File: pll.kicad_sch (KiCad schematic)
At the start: 47 parts, among them J201 S353/CDP18U42P, Q201 DTC143ZE, Q202 DTC143ZE, Q203 DTC143ZE, Q204 DTC143ZE, Q205 DTC143ZE, Q206 DTC143ZE, Q207 DTC143ZE, Q208 DTC143ZE, Q209 DTC143ZE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

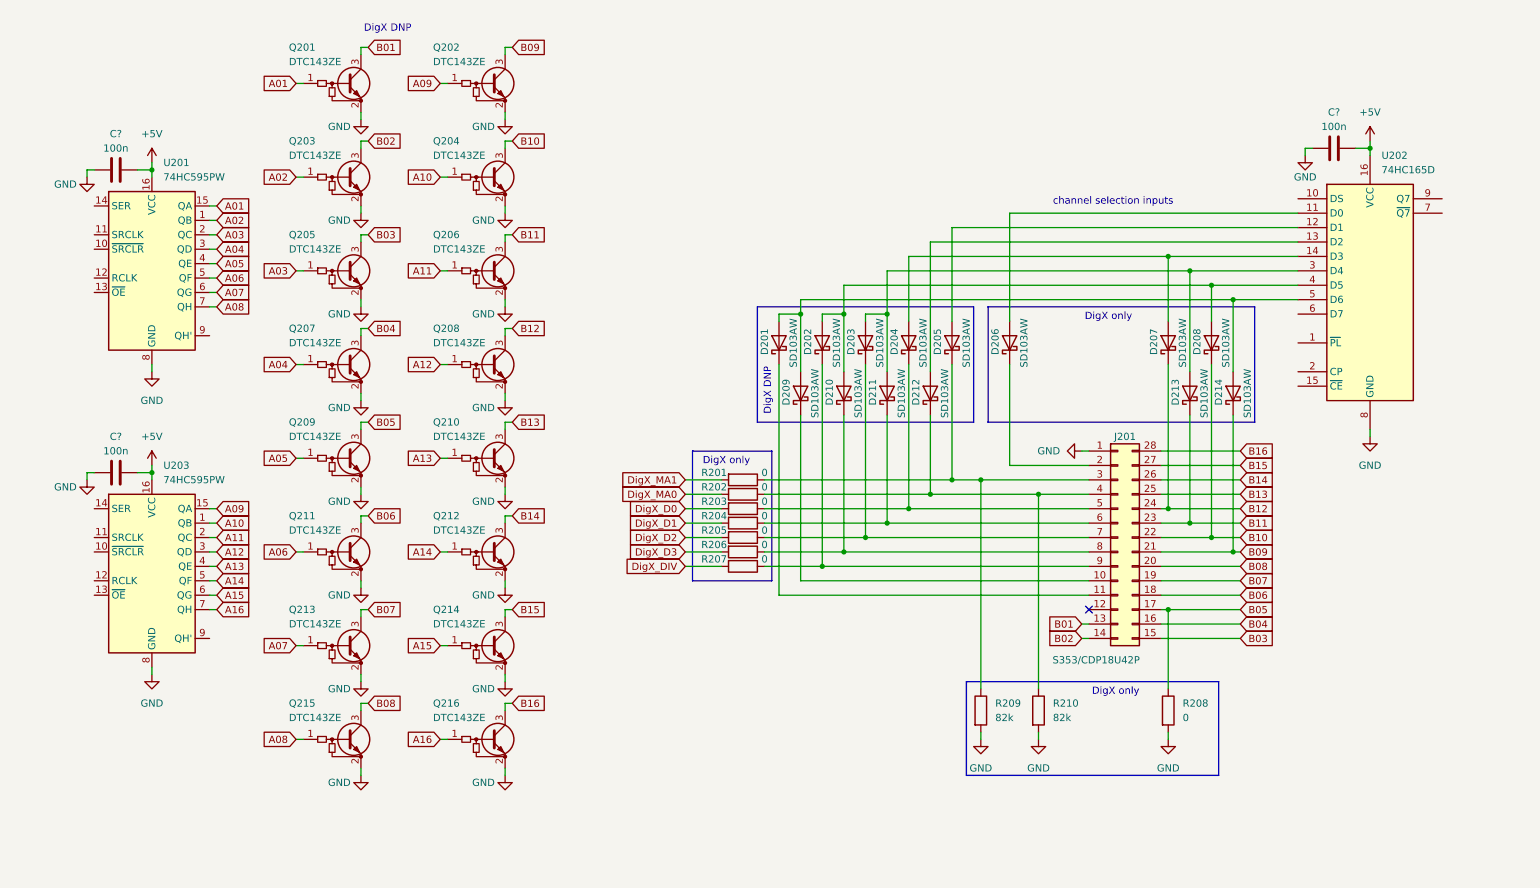
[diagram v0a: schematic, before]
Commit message: Initial TGA-connector, ESP32 and NF-filter circuit.
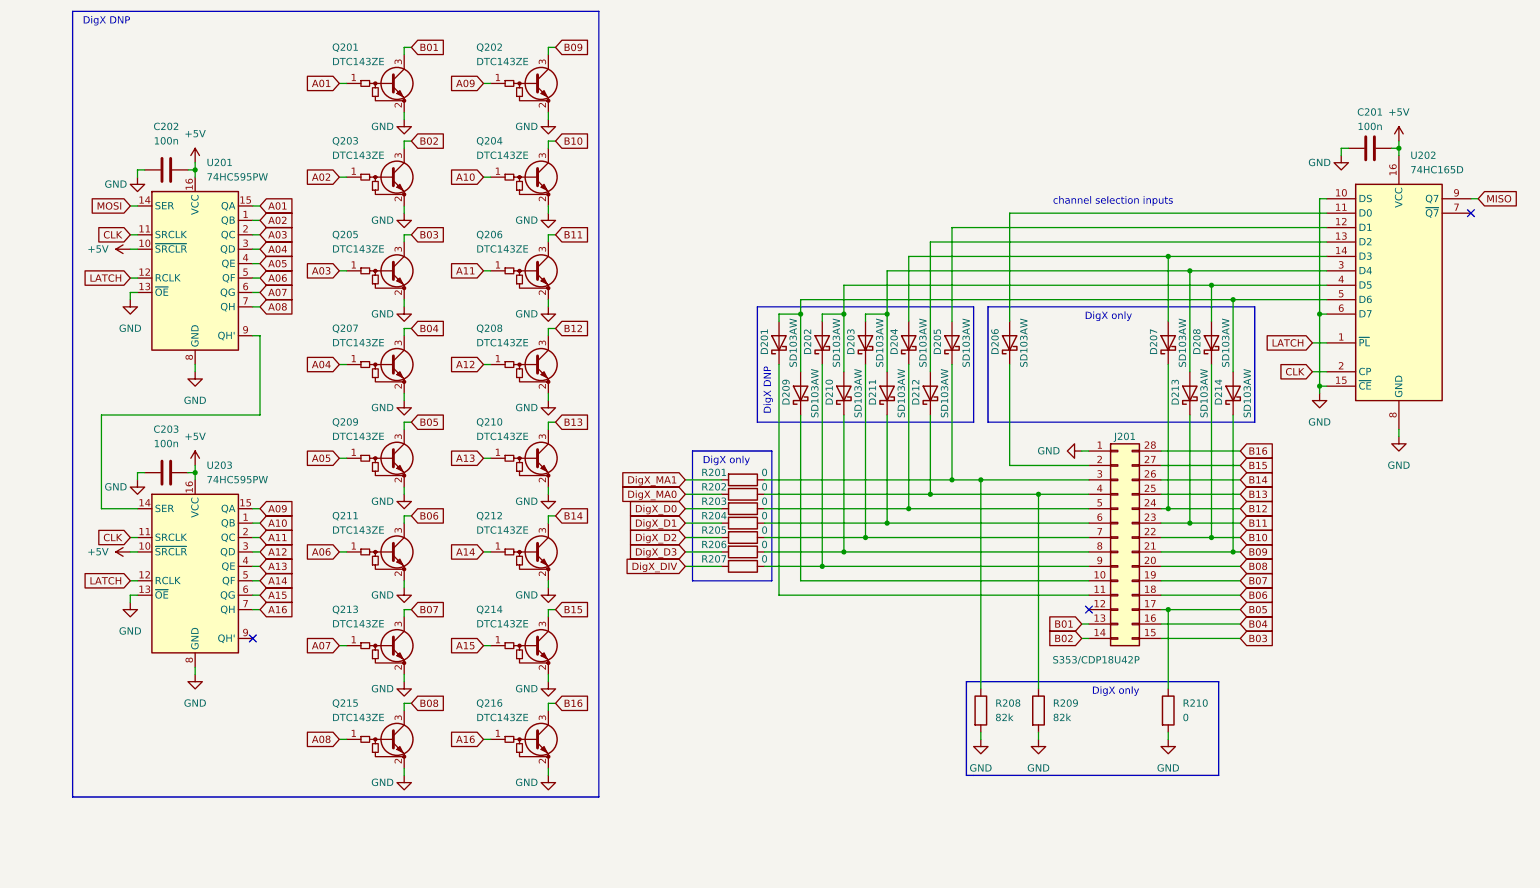
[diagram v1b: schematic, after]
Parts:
- removed C? (x2): 100n, Capacitor_SMD:C_0603_1608Metric, symbol Device:C
- added C202, C203: 100n, Capacitor_SMD:C_0603_1608Metric, symbol Device:C
- gave numbers to parts that had none: 1
- renumbered R209 to R208, R210 to R209, R208 to R210
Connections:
- net +5V: now also U201.10 (~{SRCLR}), U203.10 (~{SRCLR}), C202.2, C203.2
- net GND: now also U201.13 (~{OE}), U202.10 (DS), U202.15 (~{CE}), U202.6 (D7), U203.13 (~{OE}), C202.1, C203.1
- net CLK: now reaches U201.11 (SRCLK)
- net CLK: now also U202.2 (CP), U203.11 (SRCLK)
- net LATCH: now reaches U201.12 (RCLK)
- net LATCH: now also U202.1 (~{PL}), U203.12 (RCLK)
- net MOSI: now reaches U201.14 (SER)
- net at U201.9 (QH'): now also U203.14 (SER)
- net MISO: now reaches U202.9 (Q7)
- no-connect marks 1 -> 3
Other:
- moved on the sheet: C201, Q201, Q202, Q203, Q204, Q205, Q206, Q207, Q208, Q209, Q210, Q211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

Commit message: schematic/pcb update
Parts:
- added R201: 10k, Resistor_SMD:R_0603_1608Metric, symbol Device:R
- added R209, R211, R212, R213, R214, R217: 0, Resistor_SMD:R_0603_1608Metric, symbol Device:R
- D201, D202, D203, D204, D205, D206, D207, D208, D209, D210, D211, D212, D213, D214: footprint (none) -> Diode_SMD:D_SOD-123
- J201: footprint (none) -> Package_DIP:DIP-28_W15.24mm_LongPads
- R202, R203, R204, R205, R206, R207: value 0 -> 10k; footprint (none) -> Resistor_SMD:R_0603_1608Metric
- R208: renamed from R201; footprint (none) -> Resistor_SMD:R_0603_1608Metric; LCSC (none) -> C100044
- R210: footprint (none) -> Resistor_SMD:R_0603_1608Metric; LCSC (none) -> C100044
- R215: renamed from R208; footprint (none) -> Resistor_SMD:R_0603_1608Metric
- R216: renamed from R209; footprint (none) -> Resistor_SMD:R_0603_1608Metric
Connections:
- net B05: now also R217.1; no longer R210.1
- net DigX_D0: now also R210.2; no longer R203.2
- net DigX_D1: now also R211.2; no longer R204.2
- net DigX_D2: now also R212.2; no longer R205.2
- net DigX_D3: now also R213.2; no longer R206.2
- net DigX_DIV: now also R214.2; no longer R207.2
- net DigX_MA0: now also R209.2; no longer R202.2
- net GND: now also R217.2; no longer R210.2, U202.6 (D7)
- net at D211.1 (K), J201.6 (Pin_6): now also R211.1; no longer R204.1
- net at D204.2 (A), D207.2 (A): now also R207.2, U202.6 (D7); no longer U202.14 (D3)
- net at D212.1 (K), J201.4 (Pin_4), R216.1: now also R209.1; no longer R202.1
- net at D205.2 (A): now also R205.2, U202.4 (D5); no longer U202.12 (D1)
- net at D202.2 (A), D208.2 (A), D210.2 (A): now also R202.2, U202.12 (D1); no longer U202.4 (D5)
- net at D201.2 (A), D209.2 (A), D214.2 (A): now also U202.13 (D2), R201.2; no longer U202.5 (D6)
- net at D204.1 (K), J201.5 (Pin_5): now also R210.1; no longer R203.1
- net at D203.1 (K), J201.7 (Pin_7): now also R212.1; no longer R205.1
- net at D210.1 (K), J201.8 (Pin_8): now also R213.1; no longer R206.1
- net at D202.1 (K), J201.9 (Pin_9): now also R214.1; no longer R207.1
- net at D206.2 (A): now also R206.2, U202.3 (D4); no longer U202.11 (D0)
- net at D212.2 (A): now also R204.2, U202.5 (D6); no longer U202.13 (D2)
- net at D203.2 (A), D211.2 (A), D213.2 (A): now also R203.2, U202.11 (D0); no longer U202.3 (D4)
- net +5V renamed +3V3
- net +3V3: now also R202.1, R203.1, R204.1, R205.1, R206.1, R207.1, R201.1
- net MISO renamed MISO_PLL
- no-connect marks 3 -> 4
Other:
- moved on the sheet: C201, D201, D202, D203, D204, D205, D209, D210, D211, D212, J201, R208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

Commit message: schematic/pcb update
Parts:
- removed Q214: DTC143ZE, Package_TO_SOT_SMD:SOT-523, symbol Device:Q_NPN_BEC_BRT
- J201: LCSC (none) -> C510960
- U202: footprint Package_SO:SO-16_3.9x9.9mm_P1.27mm -> Package_SO:SOIC-16_3.9x9.9mm_P1.27mm
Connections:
- net GND: now also U202.14 (D3)
- no-connect marks 4 -> 3
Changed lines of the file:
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@@
   (junction (at 210.82 125.73) (diameter 0) (color 0 0 0 0)
   )
+  (junction (at 243.84 57.15) (diameter 0) (color 0 0 0 0)
+  )
   (junction (at 243.84 80.01) (diameter 0) (color 0 0 0 0)
   )
@@
   )
   (no_connect (at 50.8 149.86))
-  (no_connect (at 245.11 57.15))
   (no_connect (at 270.51 49.53))
   (no_connect (at 196.85 125.73))
@@
     (stroke (width 0) (type default) (color 0 0 0 0))
   )
+  (wire (pts (xy 243.84 57.15) (xy 245.11 57.15))
+    (stroke (width 0) (type default) (color 0 0 0 0))
+  )
   (wire (pts (xy 77.47 128.27) (xy 77.47 129.54))
     (stroke (width 0) (type default) (color 0 0 0 0))
@@
     (stroke (width 0) (type default) (color 0 0 0 0))
   )
+  (wire (pts (xy 243.84 57.15) (xy 243.84 80.01))
+    (stroke (width 0) (type default) (color 0 0 0 0))
+  )
   (wire (pts (xy 146.05 83.82) (xy 146.05 73.66))
     (stroke (width 0) (type default) (color 0 0 0 0))
@@
     (stroke (width 0) (type default) (color 0 0 0 0))
   )
-  (wire (pts (xy 243.84 46.99) (xy 243.84 80.01))
+  (wire (pts (xy 243.84 46.99) (xy 243.84 57.15))
     (stroke (width 0) (type default) (color 0 0 0 0))
   )
@@
     (pin "3")
   )
-  (symbol (lib_id "Device:Q_NPN_BEC_BRT") (at 101.6 151.13 0) (unit 1)
-    (in_bom yes) (on_board yes)
-    (property "Reference" "Q214" (id 0) (at 90.17 144.78 0)
-      (effects (font (size 1.27 1.27)) (justify left))
-    )
-    (property "Value" "DTC143ZE" (id 1) (at 90.17 147.32 0)
-      (effects (font (size 1.27 1.27)) (justify left))
-    )
-    (property "Footprint" "Package_TO_SOT_SMD:SOT-523" (id 2) (at 101.6 151.13 0)
-      (effects (font (size 1.27 1.27)) hide)
-    )
-    (property "Datasheet" "https://datasheet.lcsc.com/lcsc/1811071607_Tak-Cheong-DTC143ZE_C248787.pdf" (id 3) (at 101.6 151.13 0)
-      (effects (font (size 1.27 1.27)) hide)
-    )
-    (property "LCSC" "C248787" (id 4) (at 101.6 151.13 0)
-      (effects (font (size 1.27 1.27)) hide)
-    )
-    (pin "1")
-    (pin "2")
-    (pin "3")
-  )
   (symbol (lib_id "power:GND") (at 257.81 95.25 0) (unit 1)
     (in_bom yes) (on_board yes) (fields_autoplaced)
@@
       (effects (font (size 1.27 1.27)) hide)
     )
-    (property "Datasheet" "~" (id 3) (at 201.93 113.03 0)
+    (property "Datasheet" "https://datasheet.lcsc.com/lcsc/2004101131_XFCN-MH254V-11-40-1196_C510960.pdf" (id 3) (at 201.93 113.03 0)
+      (effects (font (size 1.27 1.27)) hide)
+    )
+    (property "LCSC" "C510960" (id 4) (at 201.93 113.03 0)
       (effects (font (size 1.27 1.27)) hide)
     )
@@
       (effects (font (size 1.27 1.27)) (justify left))
     )
-    (property "Footprint" "Package_SO:SO-16_3.9x9.9mm_P1.27mm" (id 2) (at 257.81 62.23 0)
-      (effects (font (size 1.27 1.27)) hide)
-    )
+    (property "Footprint" "Package_SO:SOIC-16_3.9x9.9mm_P1.27mm" (id 2) (at 257.81 62.23 0)
+      (effects (font (size 1.27 1.27)) hide)
+    )

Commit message: schematic/pcb update
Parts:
- added Q214: DTC143ZE, Package_TO_SOT_SMD:SOT-523, symbol Device:Q_NPN_BEC_BRT
- J201: footprint Package_DIP:DIP-28_W15.24mm_LongPads -> Package_DIP:DIP-28_W15.24mm_Socket_LongPads
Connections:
- net A15: now also Q214.1 (B)
- net B15: now also Q214.3 (C)
- net GND: now also Q214.2 (E)
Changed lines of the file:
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@@
     (pin "2")
+  )
+  (symbol (lib_id "Device:Q_NPN_BEC_BRT") (at 101.6 151.13 0) (unit 1)
+    (in_bom yes) (on_board yes)
+    (property "Reference" "Q214" (id 0) (at 90.17 144.78 0)
+      (effects (font (size 1.27 1.27)) (justify left))
+    )
+    (property "Value" "DTC143ZE" (id 1) (at 90.17 147.32 0)
+      (effects (font (size 1.27 1.27)) (justify left))
+    )
+    (property "Footprint" "Package_TO_SOT_SMD:SOT-523" (id 2) (at 101.6 151.13 0)
+      (effects (font (size 1.27 1.27)) hide)
+    )
+    (property "Datasheet" "https://datasheet.lcsc.com/lcsc/1811071607_Tak-Cheong-DTC143ZE_C248787.pdf" (id 3) (at 101.6 151.13 0)
+      (effects (font (size 1.27 1.27)) hide)
+    )
+    (property "LCSC" "C248787" (id 4) (at 101.6 151.13 0)
+      (effects (font (size 1.27 1.27)) hide)
+    )
+    (pin "1")
+    (pin "2")
+    (pin "3")
   )
   (symbol (lib_id "Device:D_Schottky") (at 210.82 78.74 90) (unit 1)
@@
     (property "Reference" "J201" (id 0) (at 203.2 95.25 0))
     (property "Value" "S353/CDP18U42P" (id 1) (at 198.12 134.62 0))
-    (property "Footprint" "Package_DIP:DIP-28_W15.24mm_LongPads" (id 2) (at 201.93 113.03 0)
+    (property "Footprint" "Package_DIP:DIP-28_W15.24mm_Socket_LongPads" (id 2) (at 201.93 113.03 0)
       (effects (font (size 1.27 1.27)) hide)
     )

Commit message: Finished schematic (BOM consolidation, LCSC part numbers) + sheet comments
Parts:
- C201, C202, C203: LCSC (none) -> C14663
- R201, R202, R203, R204, R205, R206, R207: value 10k -> 4.7k; LCSC (none) -> C105428
- R215, R216: LCSC (none) -> C103831
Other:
- company: (none) -> Robin Olejnik
- title: (none) -> Bosch KF163 control
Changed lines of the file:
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@@
 (kicad_sch (version 20211123) (generator eeschema)
   (paper "A4")
+  (title_block
+    (title "Bosch KF163 control")
+    (date "2022-01-20")
+    (rev "1")
+    (company "Robin Olejnik")
+    (comment 2 "License: MIT")
+    (comment 3 "www.robinolejnik.com")
+    (comment 4 "https://github.com/robinolejnik/bosch-kf163-control")
+  )
   (junction (at 146.05 73.66) (diameter 0) (color 0 0 0 0)
   )
@@
       (effects (font (size 1.27 1.27)) (justify left))
     )
-    (property "Value" "10k" (id 1) (at 185.42 41.91 0)
+    (property "Value" "4.7k" (id 1) (at 185.42 41.91 0)
       (effects (font (size 1.27 1.27)) (justify left))
     )
@@
     )
     (property "Datasheet" "~" (id 3) (at 184.15 40.64 0)
+      (effects (font (size 1.27 1.27)) hide)
+    )
+    (property "LCSC" "C105428" (id 4) (at 184.15 40.64 0)
       (effects (font (size 1.27 1.27)) hide)
     )
@@
       (effects (font (size 1.27 1.27)) hide)
     )
+    (property "LCSC" "C103831" (id 4) (at 187.96 143.51 0)
+      (effects (font (size 1.27 1.27)) hide)
+    )
     (pin "1")
     (pin "2")
@@
       (effects (font (size 1.27 1.27)) (justify left))
     )
-    (property "Value" "10k" (id 1) (at 170.18 41.91 0)
+    (property "Value" "4.7k" (id 1) (at 170.18 41.91 0)
       (effects (font (size 1.27 1.27)) (justify left))
     )
@@
     )
     (property "Datasheet" "~" (id 3) (at 168.91 40.64 0)
+      (effects (font (size 1.27 1.27)) hide)
+    )
+    (property "LCSC" "C105428" (id 4) (at 168.91 40.64 0)
       (effects (font (size 1.27 1.27)) hide)
     )
@@
     )
     (property "Datasheet" "~" (id 3) (at 252.73 38.1 0)
+      (effects (font (size 1.27 1.27)) hide)
+    )
+    (property "LCSC" "C14663" (id 4) (at 252.73 38.1 0)
       (effects (font (size 1.27 1.27)) hide)
     )
@@
       (effects (font (size 1.27 1.27)) (justify left))
     )
-    (property "Value" "10k" (id 1) (at 154.94 41.91 0)
+    (property "Value" "4.7k" (id 1) (at 154.94 41.91 0)
       (effects (font (size 1.27 1.27)) (justify left))
     )
@@
       (effects (font (size 1.27 1.27)) hide)
     )
+    (property "LCSC" "C105428" (id 4) (at 153.67 40.64 0)
+      (effects (font (size 1.27 1.27)) hide)
+    )
     (pin "1")
     (pin "2")
@@
       (effects (font (size 1.27 1.27)) (justify left))
     )
-    (property "Value" "10k" (id 1) (at 162.56 41.91 0)
+    (property "Value" "4.7k" (id 1) (at 162.56 41.91 0)
       (effects (font (size 1.27 1.27)) (justify left))
     )
@@
     )
     (property "Datasheet" "~" (id 3) (at 161.29 40.64 0)
+      (effects (font (size 1.27 1.27)) hide)
+    )
+    (property "LCSC" "C105428" (id 4) (at 161.29 40.64 0)
       (effects (font (size 1.27 1.27)) hide)
     )
@@
       (effects (font (size 1.27 1.27)) (justify left))
     )
-    (property "Value" "10k" (id 1) (at 177.8 41.91 0)
+    (property "Value" "4.7k" (id 1) (at 177.8 41.91 0)
       (effects (font (size 1.27 1.27)) (justify left))
     )
@@
     )
     (property "Datasheet" "~" (id 3) (at 176.53 40.64 0)
+      (effects (font (size 1.27 1.27)) hide)
+    )
+    (property "LCSC" "C105428" (id 4) (at 176.53 40.64 0)
       (effects (font (size 1.27 1.27)) hide)
     )
@@
       (effects (font (size 1.27 1.27)) (justify left))
     )
-    (property "Value" "10k" (id 1) (at 193.04 41.91 0)
+    (property "Value" "4.7k" (id 1) (at 193.04 41.91 0)
       (effects (font (size 1.27 1.27)) (justify left))
     )
@@
     )
     (property "Datasheet" "~" (id 3) (at 191.77 40.64 0)
+      (effects (font (size 1.27 1.27)) hide)
+    )
+    (property "LCSC" "C105428" (id 4) (at 191.77 40.64 0)
       (effects (font (size 1.27 1.27)) hide)
     )
@@
       (effects (font (size 1.27 1.27)) hide)
     )
+    (property "LCSC" "C14663" (id 4) (at 35.56 120.65 0)
+      (effects (font (size 1.27 1.27)) hide)
+    )
     (pin "1")
     (pin "2")
@@
     )
     (property "Datasheet" "~" (id 3) (at 35.56 67.31 0)
+      (effects (font (size 1.27 1.27)) hide)
+    )
+    (property "LCSC" "C14663" (id 4) (at 35.56 67.31 0)
       (effects (font (size 1.27 1.27)) hide)
     )
@@
       (effects (font (size 1.27 1.27)) hide)
     )
+    (property "LCSC" "C103831" (id 4) (at 177.8 143.51 0)
+      (effects (font (size 1.27 1.27)) hide)
+    )
     (pin "1")
     (pin "2")
@@
       (effects (font (size 1.27 1.27)) (justify left))
     )
-    (property "Value" "10k" (id 1) (at 147.32 41.91 0)
+    (property "Value" "4.7k" (id 1) (at 147.32 41.91 0)
       (effects (font (size 1.27 1.27)) (justify left))
     )
@@
       (effects (font (size 1.27 1.27)) hide)
     )
+    (property "LCSC" "C105428" (id 4) (at 146.05 40.64 0)
+      (effects (font (size 1.27 1.27)) hide)
+    )

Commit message: sheet comments, schematic variants, removed txd resistor
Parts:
- C201, R201, R202, R203, R204, R205, R206, R207, U202: variant (none) -> ControlHead
- C202, C203, Q201, Q202, Q203, Q204, Q205, Q206, Q207, Q208, Q209, Q210, Q211, Q212, Q213, Q214, Q215, Q216, U201, U203: variant (none) -> Diode
- D201, D202, D203, D204, D205, D209, D210, D211, D212: variant (none) -> ControlHead-Diode
- D206, D207, D208, D213, D214, R208, R209, R210, R211, R212, R213, R214, R215, R216, R217: variant (none) -> ControlHead-DigX
- J201: variant (none) -> Base
